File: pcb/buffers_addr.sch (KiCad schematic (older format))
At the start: 24 parts, among them U3 74LVCH162245A, U4 74LVCH162245A

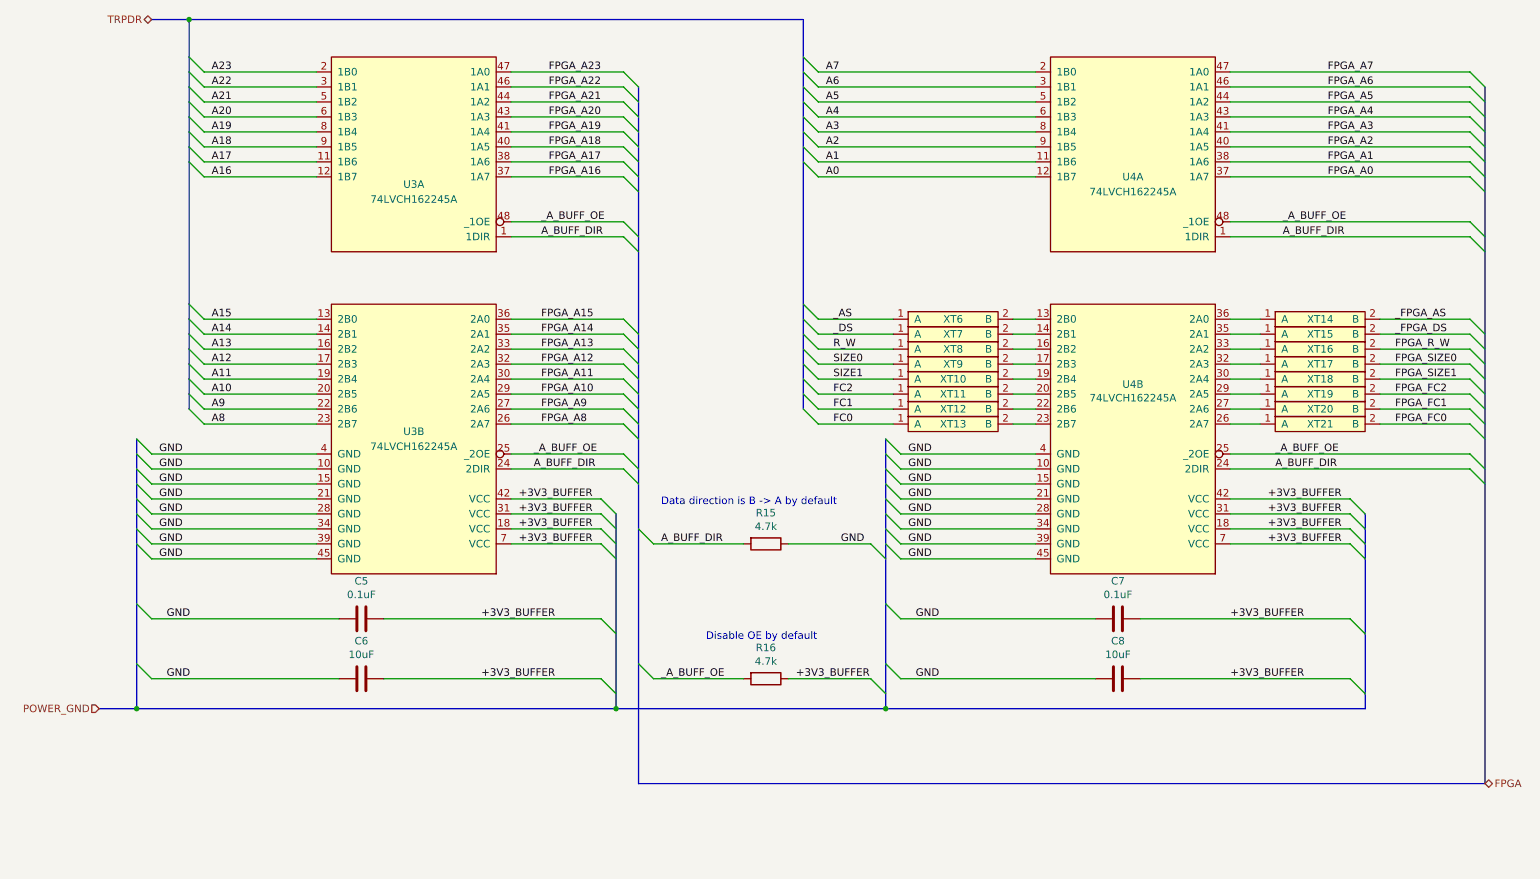
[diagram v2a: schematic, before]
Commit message: ok, we are using global labels now
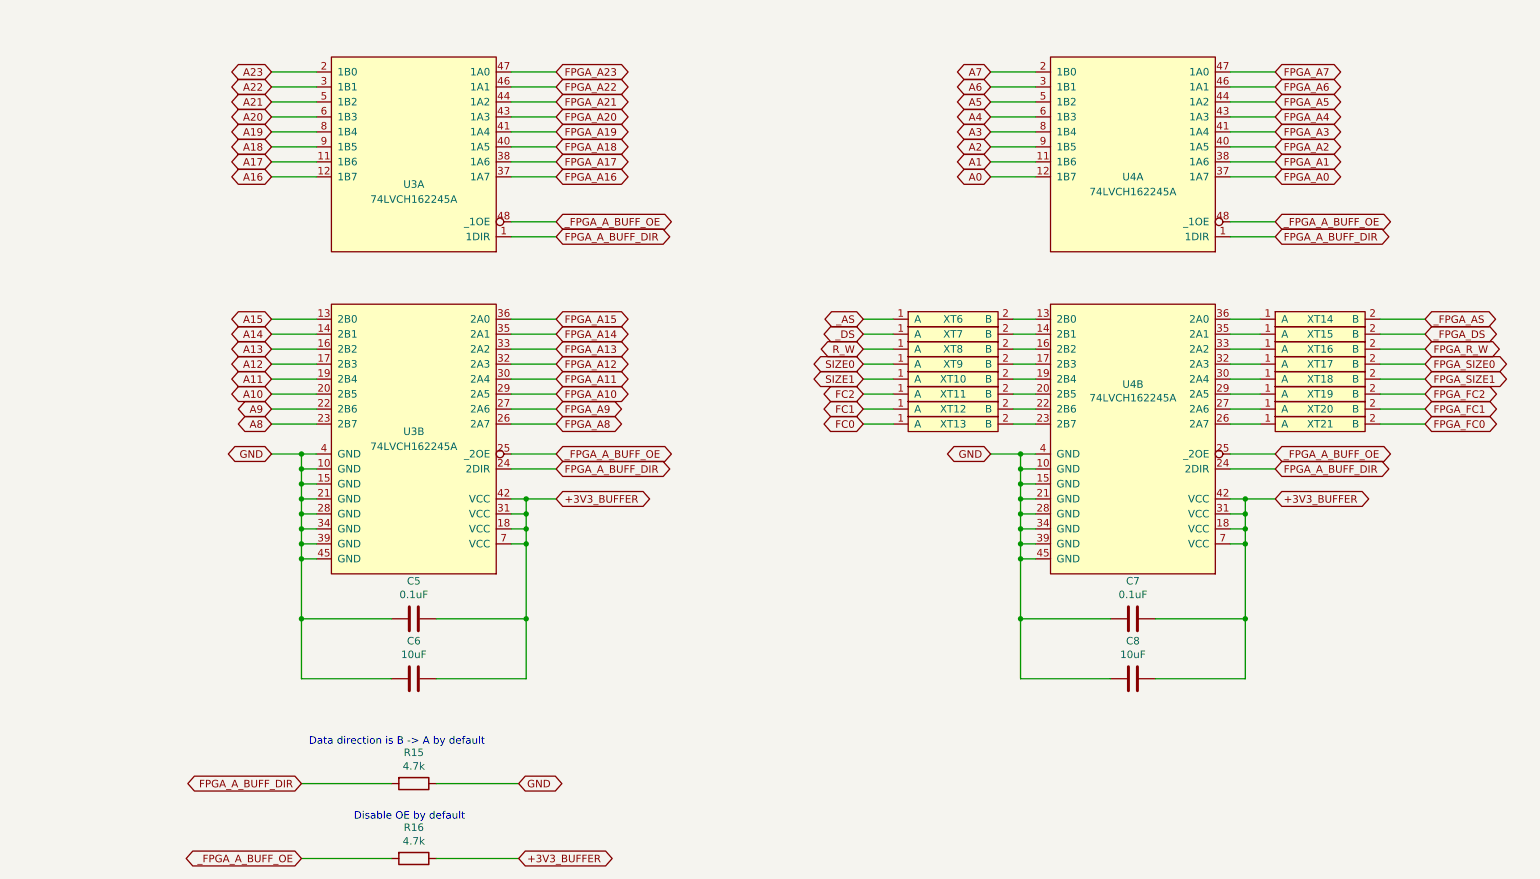
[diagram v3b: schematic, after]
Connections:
- net A_BUFF_DIR renamed FPGA_A_BUFF_DIR
- net _A_BUFF_OE renamed _FPGA_A_BUFF_OE
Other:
- moved on the sheet: C5, C6, C7, C8, R15, R16

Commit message: fpga-side gpio connector added
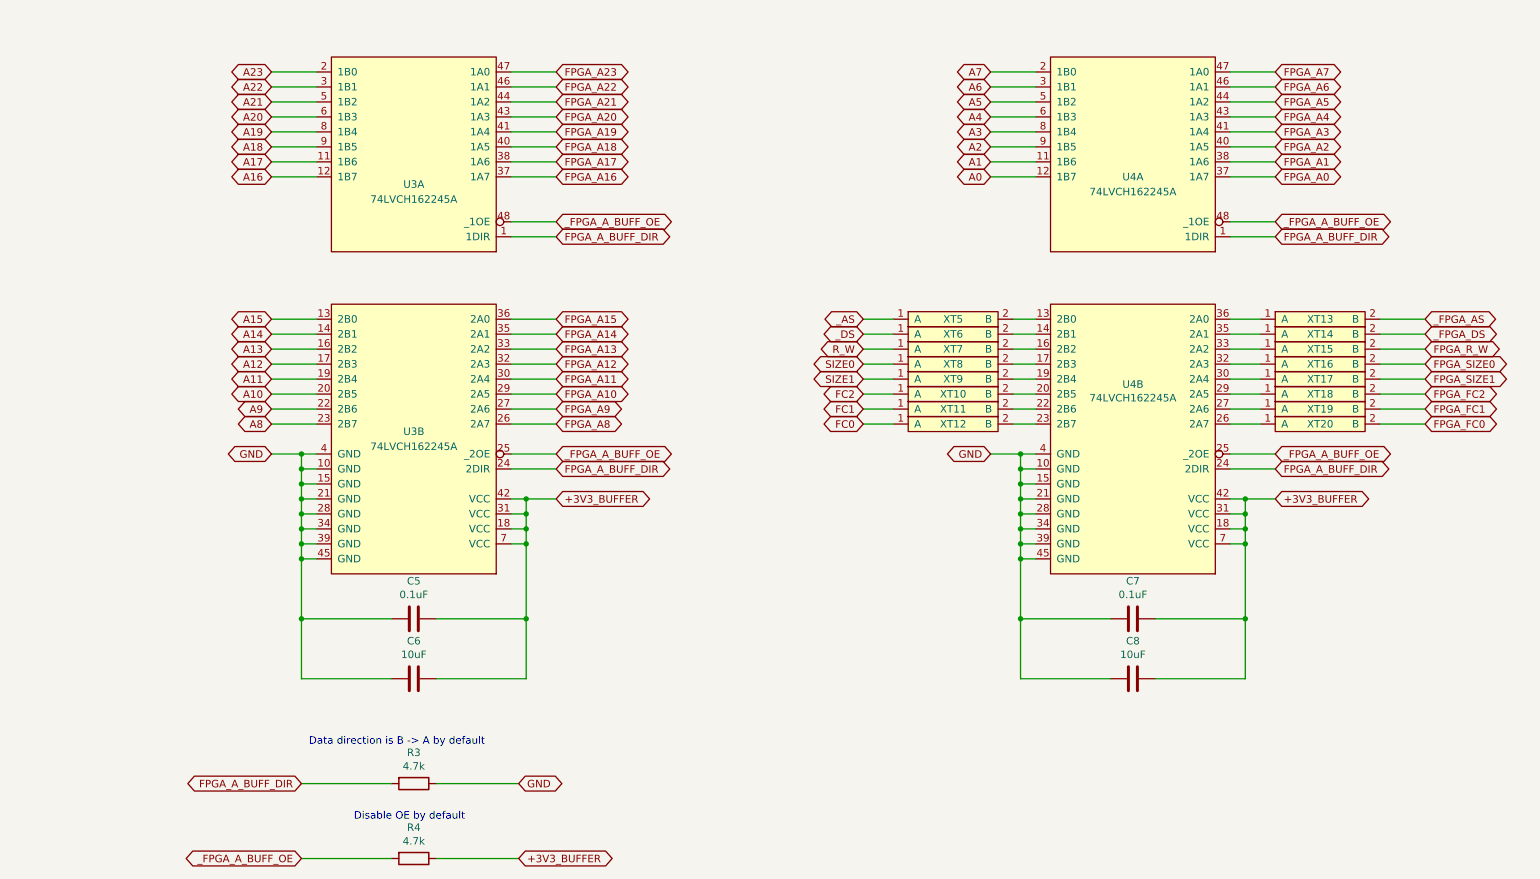
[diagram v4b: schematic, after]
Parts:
- renumbered R15 to R3, R16 to R4, XT11 to XT10, XT12 to XT11, XT13 to XT12, XT14 to XT13, XT15 to XT14, XT16 to XT15, XT17 to XT16, XT18 to XT17, XT19 to XT18, XT20 to XT19, XT21 to XT20, XT6 to XT5, XT7 to XT6, XT8 to XT7, XT9 to XT8, XT10 to XT9
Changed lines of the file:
@@
 	8200 5200 8800 5200
 $Comp
-L WM1200:testpoint_cutline XT6
+L WM1200:testpoint_cutline XT5
 U 1 1 5E57C393
 P 6850 3250
-F 0 "XT6" H 6850 3300 50  0000 C CNN
+F 0 "XT5" H 6850 3300 50  0000 C CNN
 F 1 "testpoint_cutline" H 6850 3400 50  0001 C CNN
 F 2 "" H 7000 3250 50  0001 C CNN
@@
 $EndComp
 $Comp
-L WM1200:testpoint_cutline XT7
+L WM1200:testpoint_cutline XT6
 U 1 1 5E57D0C2
 P 6850 3350
-F 0 "XT7" H 6850 3400 50  0000 C CNN
+F 0 "XT6" H 6850 3400 50  0000 C CNN
 F 1 "testpoint_cutline" H 6850 3500 50  0001 C CNN
 F 2 "" H 7000 3350 50  0001 C CNN
@@
 $EndComp
 $Comp
-L WM1200:testpoint_cutline XT8
+L WM1200:testpoint_cutline XT7
 U 1 1 5E57DCF2
 P 6850 3450
-F 0 "XT8" H 6850 3500 50  0000 C CNN
+F 0 "XT7" H 6850 3500 50  0000 C CNN
 F 1 "testpoint_cutline" H 6850 3600 50  0001 C CNN
 F 2 "" H 7000 3450 50  0001 C CNN
@@
 $EndComp
 $Comp
-L WM1200:testpoint_cutline XT9
+L WM1200:testpoint_cutline XT8
 U 1 1 5E57E315
 P 6850 3550
-F 0 "XT9" H 6850 3600 50  0000 C CNN
+F 0 "XT8" H 6850 3600 50  0000 C CNN
 F 1 "testpoint_cutline" H 6850 3700 50  0001 C CNN
 F 2 "" H 7000 3550 50  0001 C CNN
@@
 $EndComp
 $Comp
-L WM1200:testpoint_cutline XT10
+L WM1200:testpoint_cutline XT9
 U 1 1 5E57E966
 P 6850 3650
-F 0 "XT10" H 6850 3700 50  0000 C CNN
+F 0 "XT9" H 6850 3700 50  0000 C CNN
 F 1 "testpoint_cutline" H 6850 3800 50  0001 C CNN
 F 2 "" H 7000 3650 50  0001 C CNN
@@
 $EndComp
 $Comp
-L WM1200:testpoint_cutline XT11
+L WM1200:testpoint_cutline XT10
 U 1 1 5E57EE80
 P 6850 3750
-F 0 "XT11" H 6850 3800 50  0000 C CNN
+F 0 "XT10" H 6850 3800 50  0000 C CNN
 F 1 "testpoint_cutline" H 6850 3900 50  0001 C CNN
 F 2 "" H 7000 3750 50  0001 C CNN
@@
 $EndComp
 $Comp
-L WM1200:testpoint_cutline XT12
+L WM1200:testpoint_cutline XT11
 U 1 1 5E57F468
 P 6850 3850
-F 0 "XT12" H 6850 3900 50  0000 C CNN
+F 0 "XT11" H 6850 3900 50  0000 C CNN
 F 1 "testpoint_cutline" H 6850 4000 50  0001 C CNN
 F 2 "" H 7000 3850 50  0001 C CNN
@@
 $EndComp
 $Comp
-L WM1200:testpoint_cutline XT13
+L WM1200:testpoint_cutline XT12
 U 1 1 5E57FB7E
 P 6850 3950
-F 0 "XT13" H 6850 4000 50  0000 C CNN
+F 0 "XT12" H 6850 4000 50  0000 C CNN
 F 1 "testpoint_cutline" H 6850 4100 50  0001 C CNN
 F 2 "" H 7000 3950 50  0001 C CNN
@@
 P 3250 6300
 AR Path="/5E5B89F7/5E91CEB5" Ref="R?"  Part="1"
-AR Path="/5E78104B/5E91CEB5" Ref="R15"  Part="1"
-F 0 "R15" V 3043 6300 50  0000 C CNN
+AR Path="/5E78104B/5E91CEB5" Ref="R3"  Part="1"
+F 0 "R3" V 3043 6300 50  0000 C CNN
 F 1 "4.7k" V 3134 6300 50  0000 C CNN
 F 2 "" V 3180 6300 50  0001 C CNN
@@
 P 3250 6800
 AR Path="/5E5B89F7/5E91CEBB" Ref="R?"  Part="1"
-AR Path="/5E78104B/5E91CEBB" Ref="R16"  Part="1"
-F 0 "R16" V 3043 6800 50  0000 C CNN
+AR Path="/5E78104B/5E91CEBB" Ref="R4"  Part="1"
+F 0 "R4" V 3043 6800 50  0000 C CNN
 F 1 "4.7k" V 3134 6800 50  0000 C CNN
 F 2 "" V 3180 6800 50  0001 C CNN
@@
 Data direction is B -> A by default
 $Comp
-L WM1200:testpoint_cutline XT14
+L WM1200:testpoint_cutline XT13
 U 1 1 5EA42E26
 P 9300 3250
-F 0 "XT14" H 9300 3300 50  0000 C CNN
+F 0 "XT13" H 9300 3300 50  0000 C CNN
 F 1 "testpoint_cutline" H 9300 3400 50  0001 C CNN
 F 2 "" H 9450 3250 50  0001 C CNN
@@
 $EndComp
 $Comp
-L WM1200:testpoint_cutline XT15
+L WM1200:testpoint_cutline XT14
 U 1 1 5EA42E2C
 P 9300 3350
-F 0 "XT15" H 9300 3400 50  0000 C CNN
+F 0 "XT14" H 9300 3400 50  0000 C CNN
 F 1 "testpoint_cutline" H 9300 3500 50  0001 C CNN
 F 2 "" H 9450 3350 50  0001 C CNN
@@
 $EndComp
 $Comp
-L WM1200:testpoint_cutline XT16
+L WM1200:testpoint_cutline XT15
 U 1 1 5EA42E32
 P 9300 3450
-F 0 "XT16" H 9300 3500 50  0000 C CNN
+F 0 "XT15" H 9300 3500 50  0000 C CNN
 F 1 "testpoint_cutline" H 9300 3600 50  0001 C CNN
 F 2 "" H 9450 3450 50  0001 C CNN
@@
 $EndComp
 $Comp
-L WM1200:testpoint_cutline XT17
+L WM1200:testpoint_cutline XT16
 U 1 1 5EA42E38
 P 9300 3550
-F 0 "XT17" H 9300 3600 50  0000 C CNN
+F 0 "XT16" H 9300 3600 50  0000 C CNN
 F 1 "testpoint_cutline" H 9300 3700 50  0001 C CNN
 F 2 "" H 9450 3550 50  0001 C CNN
@@
 $EndComp
 $Comp
-L WM1200:testpoint_cutline XT18
+L WM1200:testpoint_cutline XT17
 U 1 1 5EA42E3E
 P 9300 3650
-F 0 "XT18" H 9300 3700 50  0000 C CNN
+F 0 "XT17" H 9300 3700 50  0000 C CNN
 F 1 "testpoint_cutline" H 9300 3800 50  0001 C CNN
 F 2 "" H 9450 3650 50  0001 C CNN
@@
 $EndComp
 $Comp
-L WM1200:testpoint_cutline XT19
+L WM1200:testpoint_cutline XT18
 U 1 1 5EA42E44
 P 9300 3750
-F 0 "XT19" H 9300 3800 50  0000 C CNN
+F 0 "XT18" H 9300 3800 50  0000 C CNN
 F 1 "testpoint_cutline" H 9300 3900 50  0001 C CNN
 F 2 "" H 9450 3750 50  0001 C CNN
@@
 $EndComp
 $Comp
-L WM1200:testpoint_cutline XT20
+L WM1200:testpoint_cutline XT19
 U 1 1 5EA42E4A
 P 9300 3850
-F 0 "XT20" H 9300 3900 50  0000 C CNN
+F 0 "XT19" H 9300 3900 50  0000 C CNN
 F 1 "testpoint_cutline" H 9300 4000 50  0001 C CNN
 F 2 "" H 9450 3850 50  0001 C CNN
@@
 $EndComp
 $Comp
-L WM1200:testpoint_cutline XT21
+L WM1200:testpoint_cutline XT20
 U 1 1 5EA42E50
 P 9300 3950
-F 0 "XT21" H 9300 4000 50  0000 C CNN
+F 0 "XT20" H 9300 4000 50  0000 C CNN
 F 1 "testpoint_cutline" H 9300 4100 50  0001 C CNN
 F 2 "" H 9450 3950 50  0001 C CNN

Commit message: testpoints footprints added, some footprints assigned
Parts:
- R3, R4: footprint (none) -> Resistor_SMD:R_0603_1608Metric_Pad1.05x0.95mm_HandSolder
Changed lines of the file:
@@
 F 0 "R3" V 3043 6300 50  0000 C CNN
 F 1 "4.7k" V 3134 6300 50  0000 C CNN
-F 2 "" V 3180 6300 50  0001 C CNN
+F 2 "Resistor_SMD:R_0603_1608Metric_Pad1.05x0.95mm_HandSolder" V 3180 6300 50  0001 C CNN
 F 3 "~" H 3250 6300 50  0001 C CNN
 	1    3250 6300
@@
 F 0 "R4" V 3043 6800 50  0000 C CNN
 F 1 "4.7k" V 3134 6800 50  0000 C CNN
-F 2 "" V 3180 6800 50  0001 C CNN
+F 2 "Resistor_SMD:R_0603_1608Metric_Pad1.05x0.95mm_HandSolder" V 3180 6800 50  0001 C CNN
 F 3 "~" H 3250 6800 50  0001 C CNN
 	1    3250 6800
